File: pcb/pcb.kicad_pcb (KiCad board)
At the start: 2 copper layers, 79 x 95 mm, 28 parts, among them J1 Screw_Terminal_01x02, J2 Screw_Terminal_01x04, J3 Screw_Terminal_01x04, Q1 2N7000, Q2 2N7000, Q3 2N7000

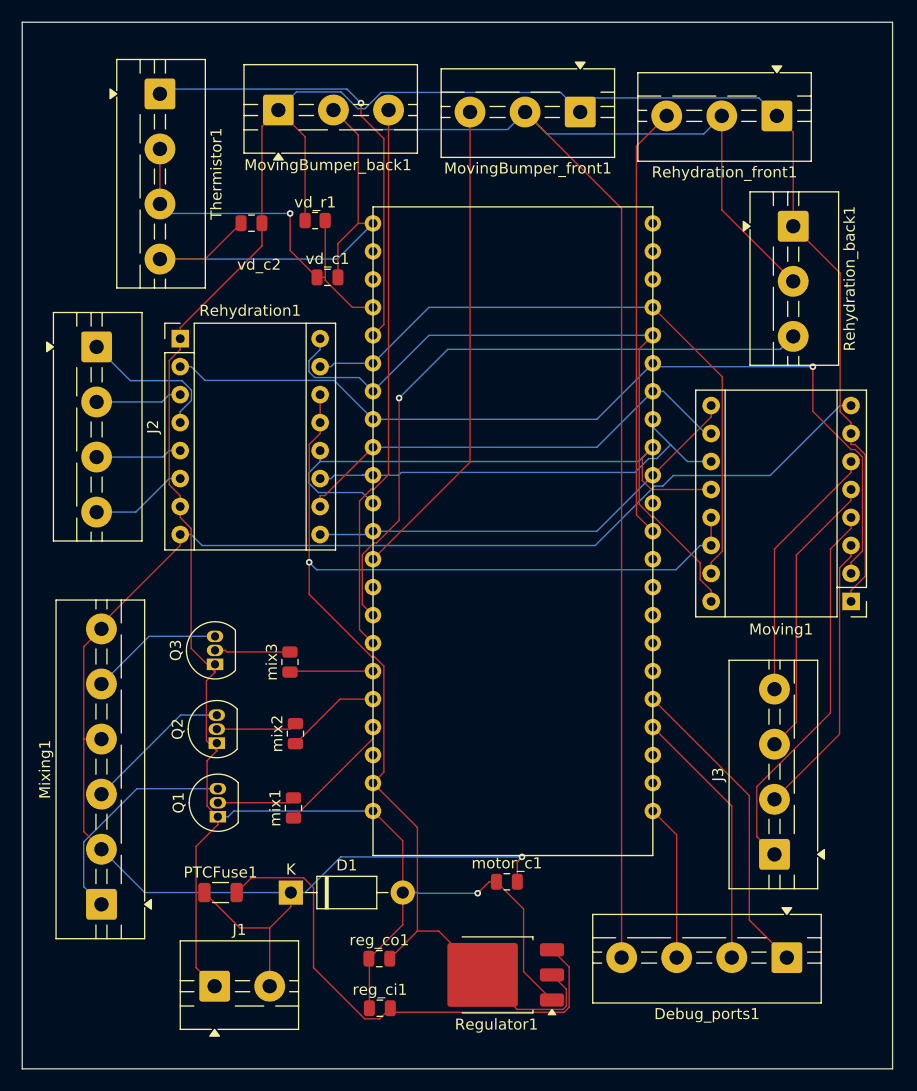
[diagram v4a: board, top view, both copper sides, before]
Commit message: forgot to pull, gonna force push this. I changed everything to through holes so we can soulder easier, added the board info onto pcb
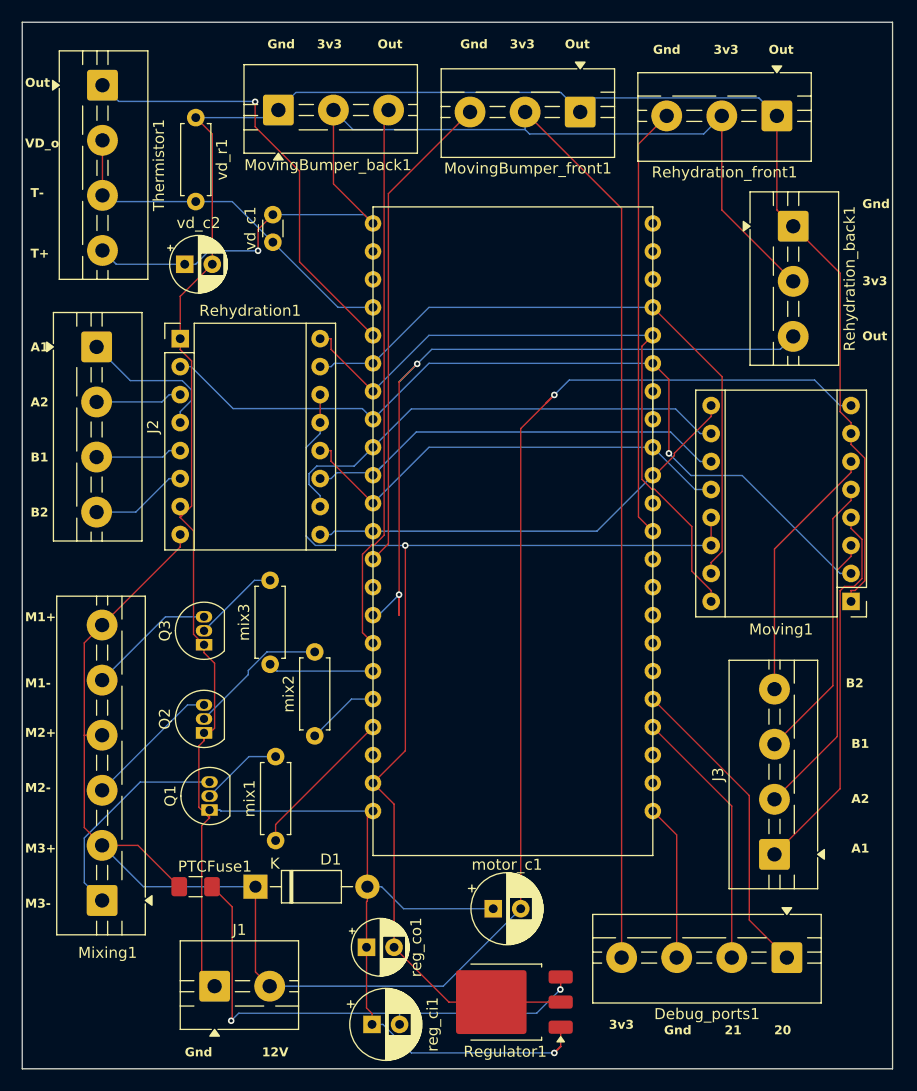
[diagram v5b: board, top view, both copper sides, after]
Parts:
- PTCFuse1: footprint Resistor_SMD:R_1206_3216Metric -> Fuse:Fuse_1206_3216Metric_Pad1.42x1.75mm_HandSolder
- mix1, mix2, mix3, vd_r1: footprint Resistor_SMD:R_0805_2012Metric -> Resistor_THT:R_Axial_DIN0207_L6.3mm_D2.5mm_P7.62mm_Horizontal
- motor_c1, reg_ci1: footprint Capacitor_SMD:C_0805_2012Metric -> Capacitor_THT:CP_Radial_D6.3mm_P2.50mm
- reg_co1, vd_c2: footprint Capacitor_SMD:C_0805_2012Metric -> Capacitor_THT:CP_Radial_D5.0mm_P2.50mm
- vd_c1: footprint Capacitor_SMD:C_0805_2012Metric -> Capacitor_THT:C_Disc_D3.0mm_W1.6mm_P2.50mm
- moved vd_r1 14.3 mm to (112.5, 58.2), turned to -90 degrees
- moved vd_c2 7.11 mm to (111.5, 71.5)
- moved vd_c1 5.90 mm to (119.5, 69.5), turned to 90 degrees
- moved Thermistor1 5.28 mm to (104.0, 55.2)
- moved mix1 3.37 mm to (119.8, 123.8)
- moved D1 3.26 mm to (117.9, 128.0)
- moved motor_c1 2.74 mm to (139.5, 130.0)
- moved Regulator1 2.59 mm to (140.6, 138.5)
- moved PTCFuse1 2.32 mm to (112.5, 128.0)
- moved Q3 2.04 mm to (113.2, 106.0)
- moved mix3 1.81 mm to (119.2, 107.8)
- moved mix2 1.76 mm to (123.3, 114.3)
- moved reg_ci1 1.63 mm to (128.5, 140.5)
- moved reg_co1 1.55 mm to (128.0, 133.5)
- moved Q2 1.48 mm to (113.2, 114.0)
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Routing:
- net /R_B: track 59.7 -> 72.0 mm, vias 1 -> 2
- net Net-(D1-K): track 163.6 -> 174.1 mm
- net /M2: track 50.7 -> 41.7 mm
- net /5V: track 117.9 -> 109.2 mm
- net Net-(Debug_ports1-Pin_4): track 183.9 -> 176.7 mm, vias 0 -> 1
- net Net-(D1-A): track 254.5 -> 261.0 mm
- net /FLT: track 82.9 -> 76.8 mm
- net Net-(Q2-G): track 7.35 -> 12.8 mm
- net /M0: track 42.0 -> 44.9 mm
- net /DIR: track 65.0 -> 62.2 mm
- net /Mix1: track 11.2 -> 14.0 mm
- net /Mix2: track 8.72 -> 6.67 mm
- net /Mix3: track 7.58 -> 9.60 mm
- net /VD_o: track 35.5 -> 33.8 mm, vias 1 -> 0
- net /Heating_pwm: track 41.3 -> 40.3 mm
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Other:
- board text added: "12V"
- board text added: "20"
- board text added: "21"
- board text added: "3v3"
- board text added: "A1"
- board text added: "A2"
- board text added: "B1"
- board text added: "B2"
- board text added: "Gnd"
- board text added: "M1+"
- board text added: "M1-"
- board text added: "M2+"
- board text added: "M2-"
- board text added: "M3+"
- board text added: "M3-"
- board text added: "Out"
- board text added: "T+"
- board text added: "T-"
- board text added: "VD_o"

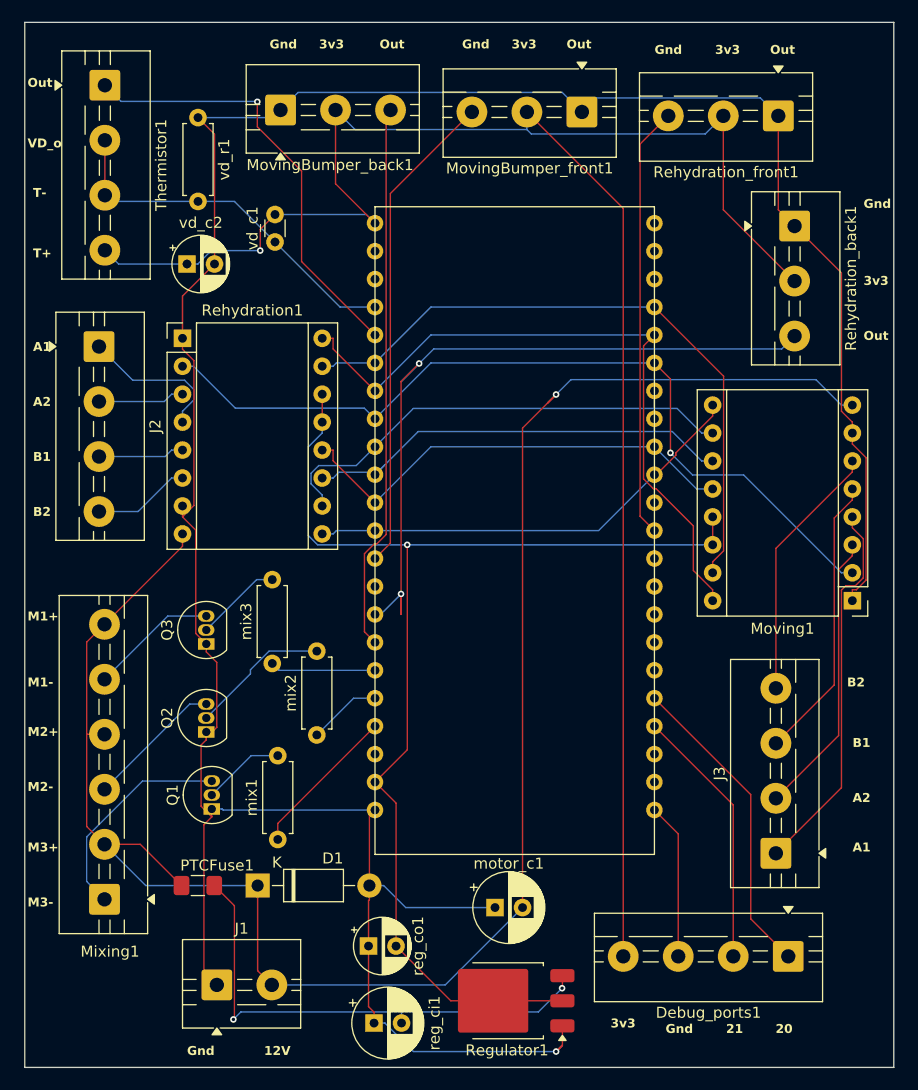
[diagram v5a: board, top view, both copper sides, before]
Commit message: edit minimum width, add copper plate
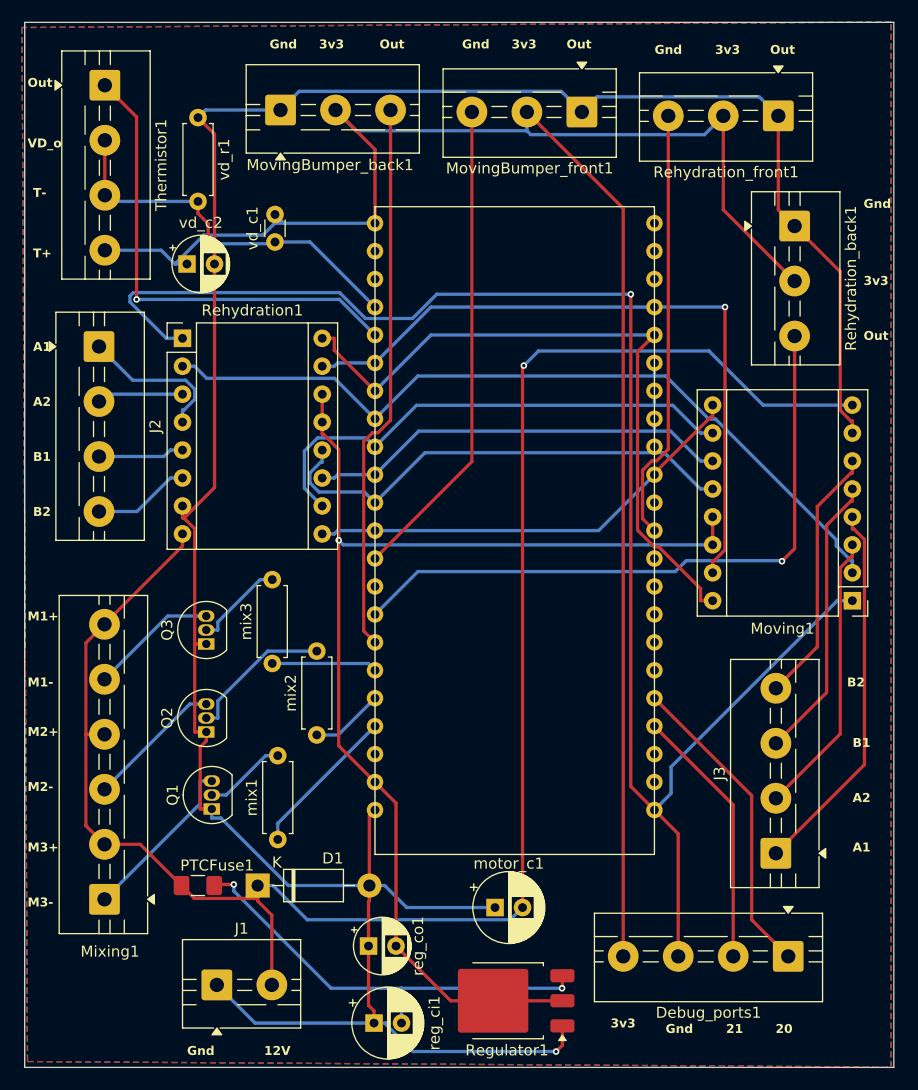
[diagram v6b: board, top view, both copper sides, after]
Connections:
- net Net-(D1-K) renamed +12V
- D1 pad 2: Net-(D1-A) -> GND
- ESP32-S3 pad 22: Net-(D1-A) -> GND
- J1 pad 1: Net-(D1-A) -> GND
- Moving1 pad 1: Net-(D1-A) -> Net-(Debug_ports1-Pin_3)
- Moving1 pad 7: Net-(D1-A) -> GND
- MovingBumper_back1 pad 1: Net-(D1-A) -> GND
- MovingBumper_front1 pad 1: Net-(D1-A) -> GND
- Q1 pad 1: Net-(D1-A) -> GND
- Q2 pad 1: Net-(D1-A) -> GND
- Q3 pad 1: Net-(D1-A) -> GND
- Regulator1 pad 1: Net-(D1-A) -> GND
- Rehydration1 pad 1: Net-(D1-A) -> Net-(Debug_ports1-Pin_3)
- Rehydration1 pad 7: Net-(D1-A) -> GND
- Rehydration_back1 pad 1: Net-(D1-A) -> GND
- Rehydration_front1 pad 1: Net-(D1-A) -> GND
- motor_c1 pad 1: Net-(D1-A) -> GND
- reg_ci1 pad 1: Net-(D1-A) -> GND
- reg_co1 pad 1: Net-(D1-A) -> GND
- vd_c2 pad 2: Net-(D1-A) -> GND
- vd_r1 pad 1: Net-(D1-A) -> GND
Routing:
- net Net-(D1-A): track 261.0 -> 0.00 mm, vias 1 -> 0
- net GND: track 0.00 -> 242.9 mm, vias 0 -> 1
- net Net-(Debug_ports1-Pin_3): track 14.2 -> 143.5 mm, vias 0 -> 1
- net /R_B: track 72.0 -> 60.0 mm, vias 2 -> 1
- net +12V: track 174.1 -> 167.5 mm
- net Net-(Regulator1-VI): track 46.4 -> 40.4 mm
- net Net-(Mixing1-Pin_1): track 19.8 -> 15.4 mm
- net /STEP: track 59.6 -> 63.6 mm, vias 0 -> 1
- net /Heating_pwm: track 40.3 -> 43.7 mm
- net /M2: track 41.7 -> 44.7 mm
- net /FLT: track 76.8 -> 74.1 mm, vias 1 -> 0
- net /M0: track 44.9 -> 47.5 mm
- net /5V: track 109.2 -> 106.9 mm
- net /VD_o: track 33.8 -> 35.6 mm, vias 0 -> 1
- net /DIR: track 62.2 -> 63.4 mm
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- added copper zone on B.Cu, net GND
- added copper zone on F.Cu, net GND

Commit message: ordered
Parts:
- added BL: MountingHole_2.2mm_M2, MountingHole:MountingHole_2.2mm_M2, F.Cu at (99.5, 142.0)
- added BR: MountingHole_2.2mm_M2, MountingHole:MountingHole_2.2mm_M2, F.Cu at (173.0, 142.0)
- added TL: MountingHole_2.2mm_M2, MountingHole:MountingHole_2.2mm_M2, F.Cu at (99.5, 52.0)
- added TR: MountingHole_2.2mm_M2, MountingHole:MountingHole_2.2mm_M2, F.Cu at (173.0, 52.0)
- moved J2 2.75 mm to (103.5, 81.8)
- moved Mixing1 2.75 mm to (104.0, 132.0)
- moved Thermistor1 2.75 mm to (104.0, 58.0)
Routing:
- net /STEP: track 63.6 -> 85.4 mm
- net Net-(Debug_ports1-Pin_3): track 143.5 -> 131.4 mm, vias 1 -> 2
- net /FLT: track 74.1 -> 84.4 mm, vias 0 -> 1
- net /M0: track 47.5 -> 42.1 mm
- net GND: track 242.9 -> 237.6 mm, vias 1 -> 0
- net +12V: track 167.5 -> 162.3 mm, vias 1 -> 0
- net /Heating_pwm: track 43.7 -> 39.0 mm
- net Net-(Regulator1-VI): track 40.4 -> 44.0 mm
- net Net-(Mixing1-Pin_1): track 15.4 -> 18.2 mm
- net /M2: track 44.7 -> 47.2 mm
- net Net-(Mixing1-Pin_3): track 12.5 -> 14.9 mm
- net /DIR: track 63.4 -> 61.0 mm, vias 0 -> 1
- net Net-(Debug_ports1-Pin_4): track 177.3 -> 175.9 mm, vias 0 -> 1
- net Net-(Mixing1-Pin_5): track 11.6 -> 12.9 mm
- net /R_B: track 60.0 -> 58.7 mm
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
